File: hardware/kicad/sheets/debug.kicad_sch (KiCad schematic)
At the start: 49 parts

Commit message: Move the IMU off-board (J14) and add labelled module boxes to the PCB
The LSM6DSOX is now the Adafruit breakout (product 4438) mounted on the
cryocooler and cabled to a 10-pin JST XH header (J14) over the shared SPI
bus. U19 and its capacitors are gone; J14 and six 100 R series resistors
are added, and every other reference number is unchanged.

PCB (130 x 110 mm, was 130 x 100):
- one outlined, labelled silkscreen box per module (pcbfloorplan.py); the
  placer keeps parts inside their box and reserves a label pocket beside
  every part so each label sits next to its own part
- box 3D models for U3, L2, L3, F1 and PS1, whose library models are missing
- re-routed; DRC 0 errors, 0 unconnected; back logo recentred
- gen_pcb.py texts redoes the silkscreen on a routed board

Firmware: SPI clock constant for the module, comments updated; ambient
temperature now reads the cooler-body IMU temperature.

Docs, BOM and fabrication files regenerated.

Co-Authored-By: Claude Sonnet 5.5 <noreply@anthropic.com>
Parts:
- removed D14: 5V (yellow), LED_SMD:LED_0603_1608Metric, symbol Device:LED
- removed D15: +15V (white), LED_SMD:LED_0603_1608Metric, symbol Device:LED
- removed D16: -15V (white), LED_SMD:LED_0603_1608Metric, symbol Device:LED
- removed TP12: -16V5, TestPoint:TestPoint_Pad_D1.5mm, symbol Connector:TestPoint
- removed TP13: ISO_3V3, TestPoint:TestPoint_Pad_D1.5mm, symbol Connector:TestPoint
- removed TP17: ISO_GND, TestPoint:TestPoint_Loop_D2.50mm_Drill1.0mm, symbol Connector:TestPoint
- removed TP18: SPI_SCK, TestPoint:TestPoint_Pad_D1.5mm, symbol Connector:TestPoint
- removed TP20: SPI_MISO, TestPoint:TestPoint_Pad_D1.5mm, symbol Connector:TestPoint
- added R86, R89: 1k, Resistor_SMD:R_0603_1608Metric, symbol Device:R_US
- added R87, R88: 4.7k, Resistor_SMD:R_0603_1608Metric, symbol Device:R_US
- added TP14, TP15: GND, TestPoint:TestPoint_Loop_D2.50mm_Drill1.0mm, symbol Connector:TestPoint
- added TP42: NTC_ADC, TestPoint:TestPoint_Pad_D1.5mm, symbol Connector:TestPoint
- added TP43: FLOW_TACH, TestPoint:TestPoint_Pad_D1.5mm, symbol Connector:TestPoint
- D14: renamed from R87; value 4.7k -> 5V (yellow); footprint Resistor_SMD:R_0603_1608Metric -> LED_SMD:LED_0603_1608Metric; symbol Device:R_US -> Device:LED
- D15: renamed from R88; value 4.7k -> +15V (white); footprint Resistor_SMD:R_0603_1608Metric -> LED_SMD:LED_0603_1608Metric; symbol Device:R_US -> Device:LED
- D16: renamed from R89; value 1k -> -15V (white); footprint Resistor_SMD:R_0603_1608Metric -> LED_SMD:LED_0603_1608Metric; symbol Device:R_US -> Device:LED
- TP12: renamed from TP14; value GND -> -16V5; footprint TestPoint:TestPoint_Loop_D2.50mm_Drill1.0mm -> TestPoint:TestPoint_Pad_D1.5mm
- TP13: renamed from TP15; value GND -> ISO_3V3; footprint TestPoint:TestPoint_Loop_D2.50mm_Drill1.0mm -> TestPoint:TestPoint_Pad_D1.5mm
- TP17: renamed from TP19; value SPI_MOSI -> ISO_GND; footprint TestPoint:TestPoint_Pad_D1.5mm -> TestPoint:TestPoint_Loop_D2.50mm_Drill1.0mm
- TP18: renamed from TP21; value MCP4921_CS -> SPI_SCK
- TP19: renamed from TP22; value AD9833_FSYNC -> SPI_MOSI
- TP20: renamed from TP23; value IMU_CS -> SPI_MISO
- TP21: renamed from TP24; value INA239_CS -> MCP4921_CS
- TP22: renamed from TP25; value ADS1220_CS -> AD9833_FSYNC
- TP23: renamed from TP26; value BRIDGE_CS -> IMU_CS
- TP24: renamed from TP27; value ACS_CS -> INA239_CS
- TP25: renamed from TP28; value ACS_MISO -> ADS1220_CS
- TP26: renamed from TP29; value BRIDGE_RESET -> BRIDGE_CS
- TP27: renamed from TP30; value SDA -> ACS_CS
- TP28: renamed from TP31; value SCL -> ACS_MISO
- TP29: renamed from TP32; value IMU_INT1 -> BRIDGE_RESET
- TP30: renamed from TP33; value IMU_INT2 -> SDA
- TP31: renamed from TP34; value FAN_ALERT -> SCL
- TP32: renamed from TP35; value PWR_KILL -> IMU_INT1
- TP33: renamed from TP36; value COMP_RELAY_EN -> IMU_INT2
- TP34: renamed from TP37; value AMP_REM_EN -> FAN_ALERT
- TP35: renamed from TP38; value UART0_TX -> PWR_KILL
- TP36: renamed from TP39; value ESP_EN -> COMP_RELAY_EN
- TP37: renamed from TP40; value ESP_BOOT -> AMP_REM_EN
- TP38: renamed from TP41; value SIG_SINE -> UART0_TX
- TP39: renamed from TP42; value NTC_ADC -> ESP_EN
- TP40: renamed from TP43; value FLOW_TACH -> ESP_BOOT
- TP41: renamed from TP44; value STATUS_RGB -> SIG_SINE
- TP44: renamed from R86; value 1k -> STATUS_RGB; footprint Resistor_SMD:R_0603_1608Metric -> TestPoint:TestPoint_Pad_D1.5mm; symbol Device:R_US -> Connector:TestPoint
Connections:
- net +15V: now also R87.1; no longer D14.1
- net +5V: now also R86.1; no longer TP44.1
- net -15V: now also R88.2; no longer D15.2
- net -16V5: now also TP12.1
- net ACS_CS: now also TP27.1; no longer TP24.1
- net ACS_MISO: now also TP28.1; no longer TP25.1
- net AD9833_FSYNC: now also TP22.1; no longer TP19.1
- net ADS1220_CS: now also TP25.1; no longer TP22.1
- net AMP_REM_EN: now also TP37.1; no longer TP34.1
- net BRIDGE_CS: now also TP26.1; no longer TP23.1
- net BRIDGE_RESET: now also TP29.1; no longer TP26.1
- net COMP_RELAY_EN: now also TP36.1; no longer TP33.1
- net ESP_BOOT: now also TP40.1; no longer TP37.1
- net ESP_EN: now also TP39.1; no longer TP36.1
- net FAN_ALERT: now also TP34.1; no longer TP31.1
- net FLOW_TACH: now also TP43.1; no longer TP40.1
- net GND: now also D14.1 (K), D15.1 (K), D16.2 (A), TP14.1, TP15.1; no longer TP12.1, TP13.1
- net IMU_CS: now also TP23.1; no longer TP20.1
- net IMU_INT1: now also TP32.1; no longer TP29.1
- net IMU_INT2: now also TP33.1; no longer TP30.1
- net INA239_CS: now also TP24.1; no longer TP21.1
- net ISO_3V3: now also TP13.1, R89.1; no longer D16.1
- net ISO_GND: now also TP17.1
- net MCP4921_CS: now also TP21.1; no longer TP18.1
- net NTC_ADC: now also TP42.1; no longer TP39.1
- net PWR_KILL: now also TP35.1; no longer TP32.1
- net SCL: now also TP31.1; no longer TP28.1
- net SDA: now also TP30.1; no longer TP27.1
- net SIG_SINE: now also TP41.1; no longer TP38.1
- net SPI_MISO: now also TP20.1
- net SPI_MOSI: now also TP19.1; no longer TP17.1
- net SPI_SCK: now also TP18.1
- net STATUS_RGB: now also TP44.1; no longer TP41.1
- net UART0_TX: now also TP38.1; no longer TP35.1
- net at D14.2 (A): now also R86.2
- net at D17.2 (A): now also R89.2; no longer D16.2
- new net: D15.2 (A), R87.2
- new net: D16.1 (K), R88.1
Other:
- moved on the sheet: D14, D15, D16, TP12, TP13, TP17, TP18, TP19, TP20, TP21, TP22, TP23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

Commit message: Add per-section supply jumpers, 8-pin IMU header and connector pin labels
- Four 1.27 mm 2-pin jumpers (JP1-JP4), each with a rail-on LED, cut the
  supply of one section for debugging: signal generator +3V3, +-15V
  generator +5V in, isolated amp-current supply +5V in, and a shared
  +3V3 net for the cooling chips (EMC2303, RTD ADC, I2C bridge).
- J14 is now an 8-pin JST XH in the Adafruit LSM6DSOX pad order
  (VIN, GND, SCL, SDA, DO, CS, I1, I2); firmware pin comments updated.
- Pin-function labels beside every connector, "RAILS ±15V" box title.
- Board re-placed and re-routed (130 x 110 mm); DRC 0 errors, 0 unconnected,
  ERC 0, 173 datasheet rules pass. BOM, READMEs, Gerbers and renders
  regenerated; link_usb_vbus.py now adapts to the routed layout.

Co-Authored-By: Claude Sonnet 5.5 <noreply@anthropic.com>
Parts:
- removed TP13: ISO_3V3, TestPoint:TestPoint_Pad_D1.5mm, symbol Connector:TestPoint
- removed TP43: FLOW_TACH, TestPoint:TestPoint_Pad_D1.5mm, symbol Connector:TestPoint
- removed TP44: STATUS_RGB, TestPoint:TestPoint_Pad_D1.5mm, symbol Connector:TestPoint
- added TP14: GND, TestPoint:TestPoint_Loop_D2.50mm_Drill1.0mm, symbol Connector:TestPoint
- added TP19: SPI_MOSI, TestPoint:TestPoint_Pad_D1.5mm, symbol Connector:TestPoint
- added TP4: VIN, TestPoint:TestPoint_Pad_D1.5mm, symbol Connector:TestPoint
- TP10: renamed from TP9; value +15V -> -15V
- TP11: renamed from TP10; value -15V -> +16V5
- TP12: renamed from TP11; value +16V5 -> -16V5
- TP13: renamed from TP12; value -16V5 -> ISO_3V3
- TP17: renamed from TP16; value GND -> ISO_GND
- TP18: renamed from TP17; value ISO_GND -> SPI_SCK; footprint TestPoint:TestPoint_Loop_D2.50mm_Drill1.0mm -> TestPoint:TestPoint_Pad_D1.5mm
- TP20: renamed from TP18; value SPI_SCK -> SPI_MISO
- TP21: renamed from TP19; value SPI_MOSI -> MCP4921_CS
- TP22: renamed from TP20; value SPI_MISO -> AD9833_FSYNC
- TP23: renamed from TP21; value MCP4921_CS -> IMU_CS
- TP24: renamed from TP22; value AD9833_FSYNC -> INA239_CS
- TP25: renamed from TP23; value IMU_CS -> ADS1220_CS
- TP26: renamed from TP24; value INA239_CS -> BRIDGE_CS
- TP27: renamed from TP25; value ADS1220_CS -> ACS_CS
- TP28: renamed from TP26; value BRIDGE_CS -> ACS_MISO
- TP29: renamed from TP27; value ACS_CS -> BRIDGE_RESET
- TP30: renamed from TP28; value ACS_MISO -> SDA
- TP31: renamed from TP29; value BRIDGE_RESET -> SCL
- TP32: renamed from TP30; value SDA -> IMU_INT1
- TP33: renamed from TP31; value SCL -> IMU_INT2
- TP34: renamed from TP32; value IMU_INT1 -> FAN_ALERT
- TP35: renamed from TP33; value IMU_INT2 -> PWR_KILL
- TP36: renamed from TP34; value FAN_ALERT -> COMP_RELAY_EN
- TP37: renamed from TP35; value PWR_KILL -> AMP_REM_EN
- TP38: renamed from TP36; value COMP_RELAY_EN -> UART0_TX
- TP39: renamed from TP37; value AMP_REM_EN -> ESP_EN
- TP40: renamed from TP38; value UART0_TX -> ESP_BOOT
- TP41: renamed from TP39; value ESP_EN -> SIG_SINE
- TP42: renamed from TP40; value ESP_BOOT -> NTC_ADC
- TP43: renamed from TP41; value SIG_SINE -> FLOW_TACH
- TP44: renamed from TP42; value NTC_ADC -> STATUS_RGB
- TP5: renamed from TP4; value VIN -> +12V
- TP6: renamed from TP5; value +12V -> VSW
- TP7: renamed from TP6; value VSW -> +5V
- TP8: renamed from TP7; value +5V -> +3V3
- TP9: renamed from TP8; value +3V3 -> +15V
- renumbered TP14 to TP15, TP15 to TP16
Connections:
- net +12V: now also TP5.1; no longer TP6.1
- net +15V: now also TP9.1; no longer TP10.1
- net +16V5: now also TP11.1; no longer TP12.1
- net +3V3: now also TP8.1; no longer TP9.1
- net +5V: now also TP7.1; no longer TP8.1
- net -15V: now also TP10.1; no longer TP11.1
- net -16V5: now also TP12.1; no longer TP13.1
- net ACS_CS: now also TP27.1; no longer TP29.1
- net ACS_MISO: now also TP28.1; no longer TP30.1
- net AD9833_FSYNC: now also TP22.1; no longer TP24.1
- net ADS1220_CS: now also TP25.1; no longer TP27.1
- net AMP_REM_EN: now also TP37.1; no longer TP39.1
- net BRIDGE_CS: now also TP26.1; no longer TP28.1
- net BRIDGE_RESET: now also TP29.1; no longer TP31.1
- net COMP_RELAY_EN: now also TP36.1; no longer TP38.1
- net ESP_BOOT: now also TP40.1; no longer TP42.1
- net ESP_EN: now also TP39.1; no longer TP41.1
- net FAN_ALERT: now also TP34.1; no longer TP36.1
- net FLOW_TACH: now also TP43.1
- net GND: now also TP14.1; no longer TP17.1
- net IMU_CS: now also TP23.1; no longer TP25.1
- net IMU_INT1: now also TP32.1; no longer TP34.1
- net IMU_INT2: now also TP33.1; no longer TP35.1
- net INA239_CS: now also TP24.1; no longer TP26.1
- net ISO_3V3: now also TP13.1
- net ISO_GND: now also TP17.1; no longer TP18.1
- net MCP4921_CS: now also TP21.1; no longer TP23.1
- net NTC_ADC: now also TP42.1; no longer TP44.1
- net PWR_KILL: now also TP35.1; no longer TP37.1
- net SCL: now also TP31.1; no longer TP33.1
- net SDA: now also TP30.1; no longer TP32.1
- net SIG_SINE: now also TP41.1; no longer TP43.1
- net SPI_MISO: now also TP20.1; no longer TP22.1
- net SPI_MOSI: now also TP19.1; no longer TP21.1
- net SPI_SCK: now also TP18.1; no longer TP20.1
- net STATUS_RGB: now also TP44.1
- net UART0_TX: now also TP38.1; no longer TP40.1
- net VIN: now also TP4.1; no longer TP5.1
- net VSW: now also TP6.1; no longer TP7.1
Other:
- moved on the sheet: TP10, TP11, TP12, TP13, TP15, TP16, TP17, TP18, TP20, TP21, TP22, TP23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

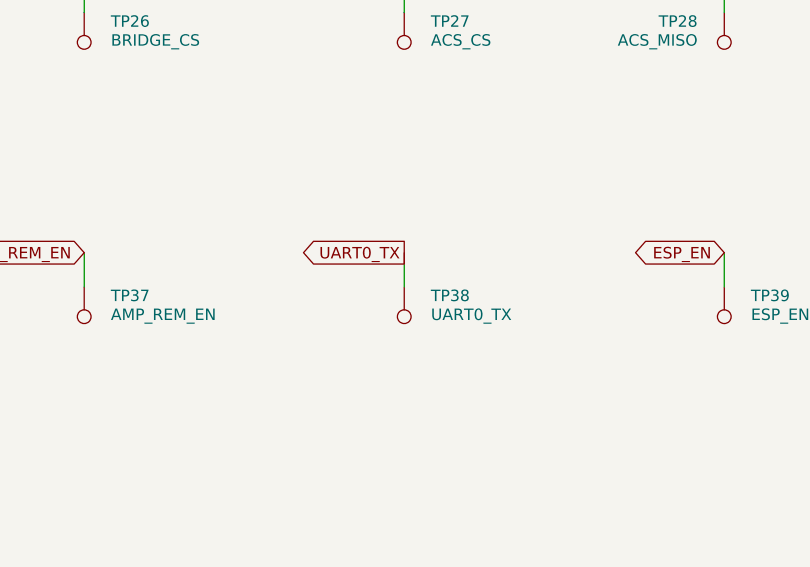
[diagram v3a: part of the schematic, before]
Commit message: Replace the ±15 V LDOs with one LT3097 and add a power-good interlock
- rails_15v: ADP7142 + ADP7182 replaced by one LT3097 (±14.7 V, 147 k SET
  resistors); the ADP5071 output caps are now 22 uF / 50 V and double as the
  LT3097 inputs. PGP / PGN make the PG_15V node (fed from +15 V, so it reads
  0 V if a rail is missing).
- amp_control: a series BSS138 (Q9) gated by PG_15V blocks AMP_REM unless
  both rails are good. New power_good sheet: LED (D23) and the active-low
  PG_15V_N flag on GPIO43 (PG_15V_N_PIN).
- Tooling: LT3097 symbol, footprint and 3D envelope; datasheet rules (191),
  GPIO check, BOM tables, floor plan, PAD_BRIDGES and pre-placed GND vias in
  gen_pcb.py, new fix_route.py for post-route clean-up.
- Board regenerated and routed with Freerouting 2.5.0: DRC 0 unconnected,
  0 schematic-parity issues, no copper violations. Gerbers, JLCPCB zip,
  renders, BOM, CPL and schematic PDF regenerated.

Co-Authored-By: Claude Sonnet 5.5 <noreply@anthropic.com>
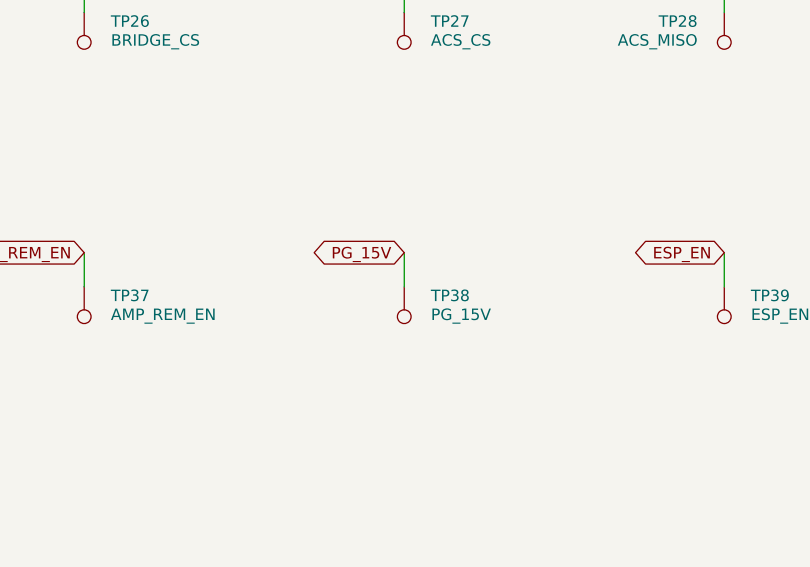
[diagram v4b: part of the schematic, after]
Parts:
- removed TP10: -15V, TestPoint:TestPoint_Pad_D1.5mm, symbol Connector:TestPoint
- removed TP11: +16V5, TestPoint:TestPoint_Pad_D1.5mm, symbol Connector:TestPoint
- removed TP12: -16V5, TestPoint:TestPoint_Pad_D1.5mm, symbol Connector:TestPoint
- removed TP13: ISO_3V3, TestPoint:TestPoint_Pad_D1.5mm, symbol Connector:TestPoint
- removed TP19: SPI_MOSI, TestPoint:TestPoint_Pad_D1.5mm, symbol Connector:TestPoint
- removed TP21: MCP4921_CS, TestPoint:TestPoint_Pad_D1.5mm, symbol Connector:TestPoint
- removed TP24: INA239_CS, TestPoint:TestPoint_Pad_D1.5mm, symbol Connector:TestPoint
- removed TP26: BRIDGE_CS, TestPoint:TestPoint_Pad_D1.5mm, symbol Connector:TestPoint
- removed TP28: ACS_MISO, TestPoint:TestPoint_Pad_D1.5mm, symbol Connector:TestPoint
- removed TP30: SDA, TestPoint:TestPoint_Pad_D1.5mm, symbol Connector:TestPoint
- removed TP7: +5V, TestPoint:TestPoint_Pad_D1.5mm, symbol Connector:TestPoint
- removed TP8: +3V3, TestPoint:TestPoint_Pad_D1.5mm, symbol Connector:TestPoint
- removed TP9: +15V, TestPoint:TestPoint_Pad_D1.5mm, symbol Connector:TestPoint
- added D14: 5V (yellow), LED_SMD:LED_0603_1608Metric, symbol Device:LED
- added D15: +15V (white), LED_SMD:LED_0603_1608Metric, symbol Device:LED
- added D16: -15V (white), LED_SMD:LED_0603_1608Metric, symbol Device:LED
- added D17: ISO 3V3 (green), LED_SMD:LED_0603_1608Metric, symbol Device:LED
- added R87, R88: 4.7k, Resistor_SMD:R_0603_1608Metric, symbol Device:R_US
- added TP32: IMU_INT1, TestPoint:TestPoint_Pad_D1.5mm, symbol Connector:TestPoint
- added TP33: IMU_INT2, TestPoint:TestPoint_Pad_D1.5mm, symbol Connector:TestPoint
- added TP36: COMP_RELAY_EN, TestPoint:TestPoint_Pad_D1.5mm, symbol Connector:TestPoint
- added TP37: AMP_REM_EN, TestPoint:TestPoint_Pad_D1.5mm, symbol Connector:TestPoint
- added TP40: ESP_BOOT, TestPoint:TestPoint_Pad_D1.5mm, symbol Connector:TestPoint
- added TP41: SIG_SINE, TestPoint:TestPoint_Pad_D1.5mm, symbol Connector:TestPoint
- added TP44: STATUS_RGB, TestPoint:TestPoint_Pad_D1.5mm, symbol Connector:TestPoint
- R86: renamed from D17; value ISO 3V3 (green) -> 1k; footprint LED_SMD:LED_0603_1608Metric -> Resistor_SMD:R_0603_1608Metric; symbol Device:LED -> Device:R_US
- TP10: renamed from TP17; value ISO_GND -> -15V; footprint TestPoint:TestPoint_Loop_D2.50mm_Drill1.0mm -> TestPoint:TestPoint_Pad_D1.5mm
- TP11: renamed from TP18; value SPI_SCK -> +16V5
- TP12: renamed from TP20; value SPI_MISO -> -16V5
- TP13: renamed from TP22; value AD9833_FSYNC -> ISO_3V3
- TP14: renamed from TP23; value IMU_CS -> GND; footprint TestPoint:TestPoint_Pad_D1.5mm -> TestPoint:TestPoint_Loop_D2.50mm_Drill1.0mm
- TP15: renamed from TP25; value ADS1220_CS -> GND; footprint TestPoint:TestPoint_Pad_D1.5mm -> TestPoint:TestPoint_Loop_D2.50mm_Drill1.0mm
- TP16: renamed from TP27; value ACS_CS -> GND; footprint TestPoint:TestPoint_Pad_D1.5mm -> TestPoint:TestPoint_Loop_D2.50mm_Drill1.0mm
- TP17: renamed from TP29; value BRIDGE_RESET -> ISO_GND; footprint TestPoint:TestPoint_Pad_D1.5mm -> TestPoint:TestPoint_Loop_D2.50mm_Drill1.0mm
- TP18: renamed from TP31; value SCL -> SPI_SCK
- TP19: renamed from TP32; value IMU_INT1 -> SPI_MOSI
- TP20: renamed from TP33; value IMU_INT2 -> SPI_MISO
- TP21: renamed from TP34; value FAN_ALERT -> MCP4921_CS
- TP22: renamed from TP35; value PWR_KILL -> AD9833_FSYNC
- TP23: renamed from TP36; value COMP_RELAY_EN -> IMU_CS
- TP24: renamed from TP37; value AMP_REM_EN -> INA239_CS
- TP25: renamed from TP38; value UART0_TX -> ADS1220_CS
- TP26: renamed from TP39; value ESP_EN -> BRIDGE_CS
- TP27: renamed from TP40; value ESP_BOOT -> ACS_CS
- TP28: renamed from TP41; value SIG_SINE -> ACS_MISO
- TP29: renamed from TP42; value NTC_ADC -> BRIDGE_RESET
- TP30: renamed from TP43; value FLOW_TACH -> SDA
- TP31: renamed from TP44; value STATUS_RGB -> SCL
- TP34: renamed from R86; value 1k -> FAN_ALERT; footprint Resistor_SMD:R_0603_1608Metric -> TestPoint:TestPoint_Pad_D1.5mm; symbol Device:R_US -> Connector:TestPoint
- TP35: renamed from D14; value 5V (yellow) -> PWR_KILL; footprint LED_SMD:LED_0603_1608Metric -> TestPoint:TestPoint_Pad_D1.5mm; symbol Device:LED -> Connector:TestPoint
- TP38: renamed from R87; value 4.7k -> PG_15V; footprint Resistor_SMD:R_0603_1608Metric -> TestPoint:TestPoint_Pad_D1.5mm; symbol Device:R_US -> Connector:TestPoint
- TP39: renamed from D15; value +15V (white) -> ESP_EN; footprint LED_SMD:LED_0603_1608Metric -> TestPoint:TestPoint_Pad_D1.5mm; symbol Device:LED -> Connector:TestPoint
- TP42: renamed from R88; value 4.7k -> NTC_ADC; footprint Resistor_SMD:R_0603_1608Metric -> TestPoint:TestPoint_Pad_D1.5mm; symbol Device:R_US -> Connector:TestPoint
- TP43: renamed from D16; value -15V (white) -> FLOW_TACH; footprint LED_SMD:LED_0603_1608Metric -> TestPoint:TestPoint_Pad_D1.5mm; symbol Device:LED -> Connector:TestPoint
- TP7: renamed from TP14; value GND -> +5V; footprint TestPoint:TestPoint_Loop_D2.50mm_Drill1.0mm -> TestPoint:TestPoint_Pad_D1.5mm
- TP8: renamed from TP15; value GND -> +3V3; footprint TestPoint:TestPoint_Loop_D2.50mm_Drill1.0mm -> TestPoint:TestPoint_Pad_D1.5mm
- TP9: renamed from TP16; value GND -> +15V; footprint TestPoint:TestPoint_Loop_D2.50mm_Drill1.0mm -> TestPoint:TestPoint_Pad_D1.5mm
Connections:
- net UART0_TX is gone; now on net ADS1220_CS: TP25.1
- net +15V: now also TP9.1, R87.1; no longer TP38.1
- net +16V5: now also TP11.1
- net +3V3: now also TP8.1
- net +5V: now also R86.1, TP7.1; no longer TP34.1
- net -15V: now also TP10.1, R88.2; no longer TP42.2
- net -16V5: now also TP12.1
- net ACS_CS: now also TP27.1; no longer TP16.1
- net ACS_MISO: now also TP28.1
- net AD9833_FSYNC: now also TP22.1; no longer TP13.1
- net ADS1220_CS: no longer TP15.1
- net AMP_REM_EN: now also TP37.1; no longer TP24.1
- net BRIDGE_CS: now also TP26.1
- net BRIDGE_RESET: now also TP29.1; no longer TP17.1
- net COMP_RELAY_EN: now also TP36.1; no longer TP23.1
- net ESP_BOOT: now also TP40.1; no longer TP27.1
- net ESP_EN: now also TP39.1; no longer TP26.1
- net FAN_ALERT: now also TP34.1; no longer TP21.1
- net FLOW_TACH: now also TP43.1; no longer TP30.1
- net GND: now also TP14.1, TP15.1, TP16.1, D14.1 (K), D15.1 (K), D16.2 (A); no longer TP35.1 (K), TP39.1 (K), TP43.2 (A), TP7.1, TP8.1, TP9.1
- net IMU_CS: now also TP23.1; no longer TP14.1
- net IMU_INT1: now also TP32.1; no longer TP19.1
- net IMU_INT2: now also TP33.1; no longer TP20.1
- net INA239_CS: now also TP24.1
- net ISO_3V3: now also TP13.1
- net ISO_GND: now also TP17.1, D17.1 (K); no longer R86.1 (K), TP10.1
- net MCP4921_CS: now also TP21.1
- net NTC_ADC: now also TP42.1; no longer TP29.1
- net PWR_KILL: now also TP35.1; no longer TP22.1
- net SCL: now also TP31.1; no longer TP18.1
- net SDA: now also TP30.1
- net SIG_SINE: now also TP41.1; no longer TP28.1
- net SPI_MISO: now also TP20.1; no longer TP12.1
- net SPI_MOSI: now also TP19.1
- net SPI_SCK: now also TP18.1; no longer TP11.1
- net STATUS_RGB: now also TP44.1; no longer TP31.1
- net at R89.2: now also D17.2 (A); no longer R86.2 (A)
- new net: D15.2 (A), R87.2
- new net: D14.2 (A), R86.2
- new net: D16.1 (K), R88.1
- new net PG_15V: TP38.1
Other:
- moved on the sheet: R86, TP10, TP11, TP12, TP13, TP14, TP15, TP16, TP17, TP18, TP19, TP20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
